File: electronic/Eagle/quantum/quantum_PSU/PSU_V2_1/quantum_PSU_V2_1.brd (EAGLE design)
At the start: 92.5 x 150 mm, 37 parts, among them J1 90814-0204, J2 90814-0204, J3 PF0030_PC, U1 7815, U2 7812, U3 7915, U4 7805, U5 LD1117AV33

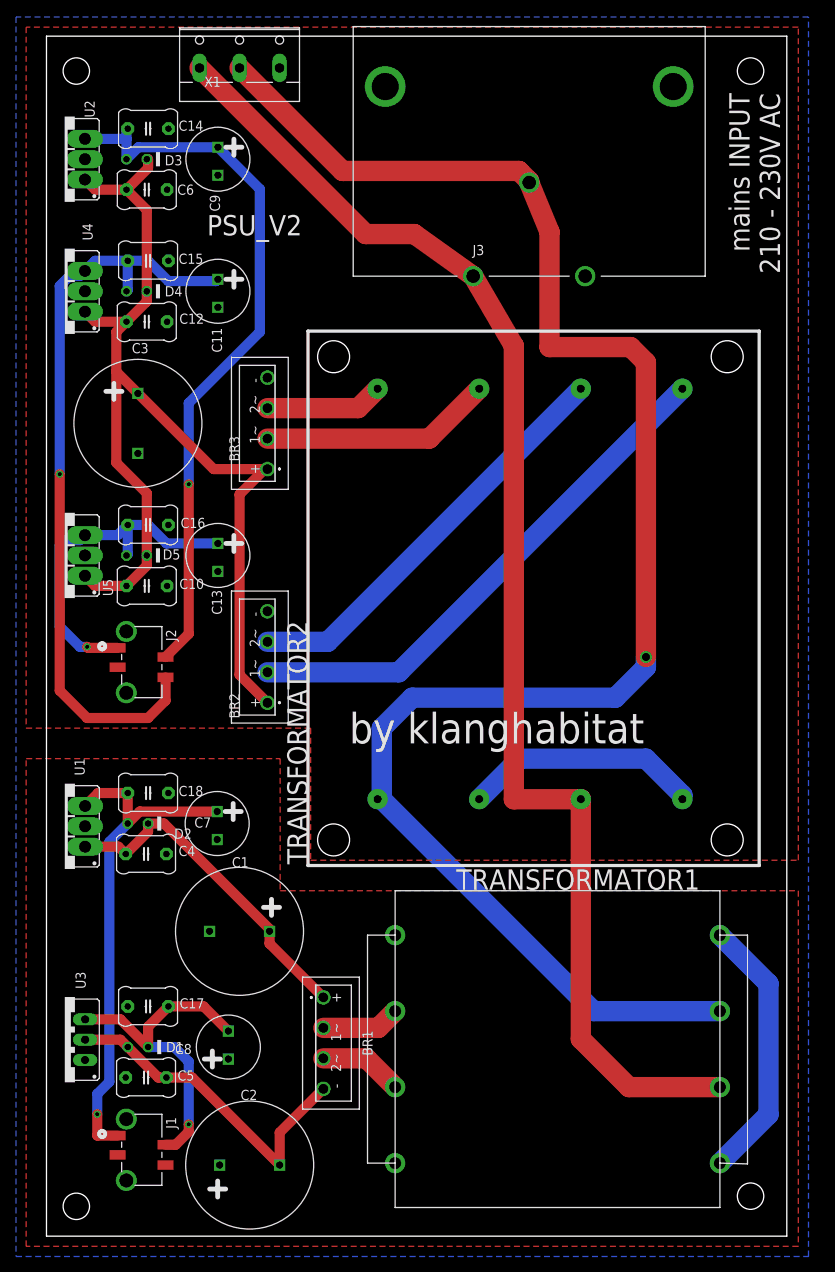
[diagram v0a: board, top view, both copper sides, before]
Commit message: several mockups and changes during debugging AnalougeEngine_V5_0. Implemented DSP functionality + rudimental FFT function
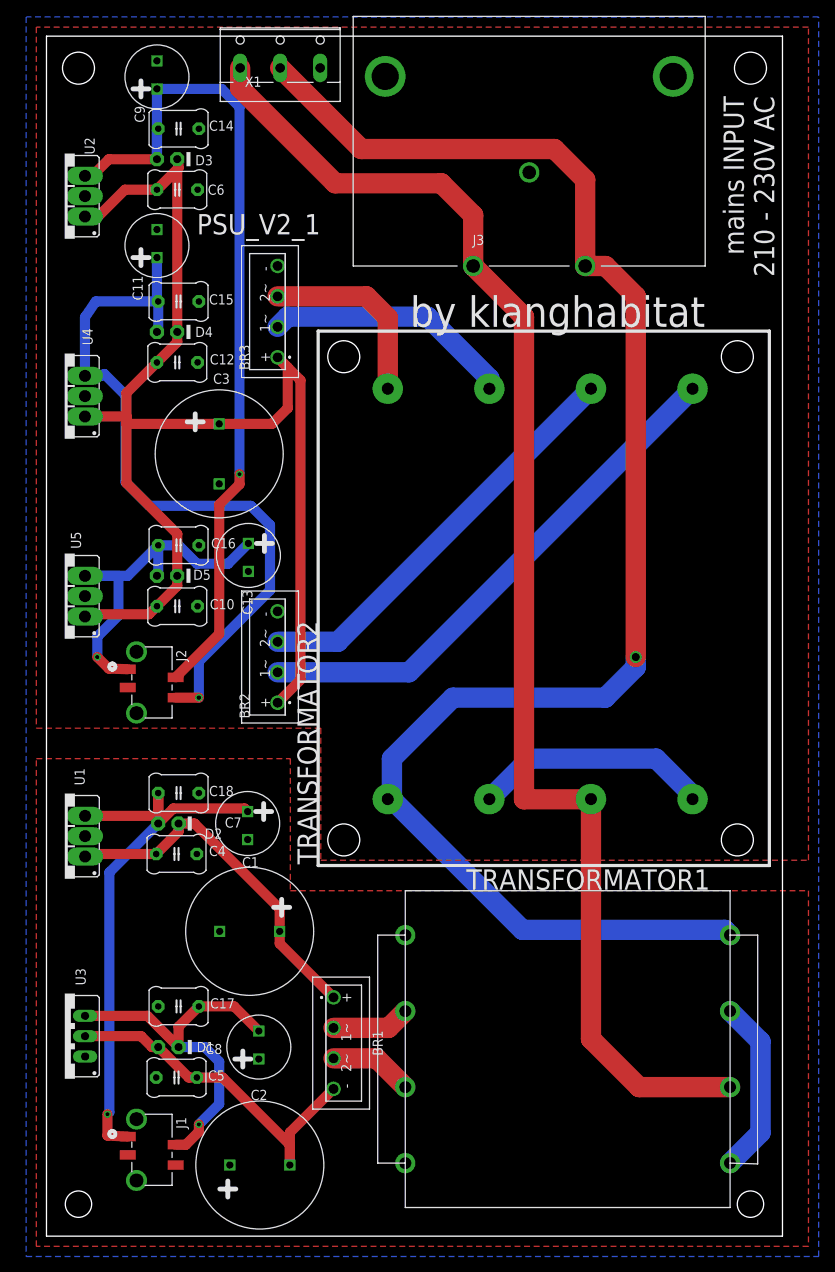
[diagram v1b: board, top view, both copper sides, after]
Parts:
- moved BR3 14.0 mm to (27.9, 115.6)
- moved U4 13.1 mm to (2.27, 105.0)
- moved C9 12.8 mm to (13.8, 144.9), turned to 90 degrees
- moved C3 10.9 mm to (21.6, 97.8)
- moved C11 9.53 mm to (13.8, 123.8), turned to 90 degrees
- moved C12 6.35 mm to (15.1, 109.2)
- moved C15 6.35 mm to (15.2, 116.8)
- moved D4 6.35 mm to (13.8, 113.0)
- moved U5 5.09 mm to (2.27, 80.0)
- moved X1 5.08 mm to (29.2, 147.3)
- moved U2 4.62 mm to (2.27, 130.0)
- moved C10 4.58 mm to (15.1, 78.7)
- moved C16 4.58 mm to (15.2, 86.4)
- moved D5 4.58 mm to (13.8, 82.5)
- moved C7 3.81 mm to (25.1, 51.6)
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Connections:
- net N$4: now also TRANSFORMATOR1.P$3; no longer TRANSFORMATOR1.P$4
- net N$8: now also TRANSFORMATOR1.P$4; no longer TRANSFORMATOR1.P$3
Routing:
- net N$2: track 133.2 -> 168.1 mm
- net +12V_OUT: track 91.9 -> 108.3 mm
- net N$8: track 213.1 -> 199.1 mm
- net N$4: track 33.5 -> 22.2 mm
- net N$1: track 14.8 -> 23.8 mm
- net +15V_OUT: track 64.7 -> 72.1 mm
- net -15V_OUT: track 42.4 -> 47.4 mm
- net +3V3_OUT: track 44.2 -> 47.9 mm
- net N$17: track 42.6 -> 45.5 mm
- net +5V_OUT: track 95.1 -> 92.5 mm
- net N$9: track 169.5 -> 172.1 mm
- net N$15: track 42.4 -> 44.9 mm
- net N$6: track 29.1 -> 31.5 mm
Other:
- board size 92.5 x 150 mm -> 92 x 150 mm
- board text added: "PSU_V2_1"
- board text removed: "PSU_V2"
